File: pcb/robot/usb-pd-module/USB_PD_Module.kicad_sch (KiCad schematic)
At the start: 57 parts, among them J4 USB4151-GF-C, J9 Conn_01x16, U11 MAX77958EWV+T, U15 TPD1E05U06, U16 fpf1048bucx, U17 TPS61253AYFFT, U19 TPD1E05U06, U20 TPD1E05U06, U21 TPD1E05U06, U22 TPD1E05U06, U23 TPD1E05U06, U24 TVS0500DRV

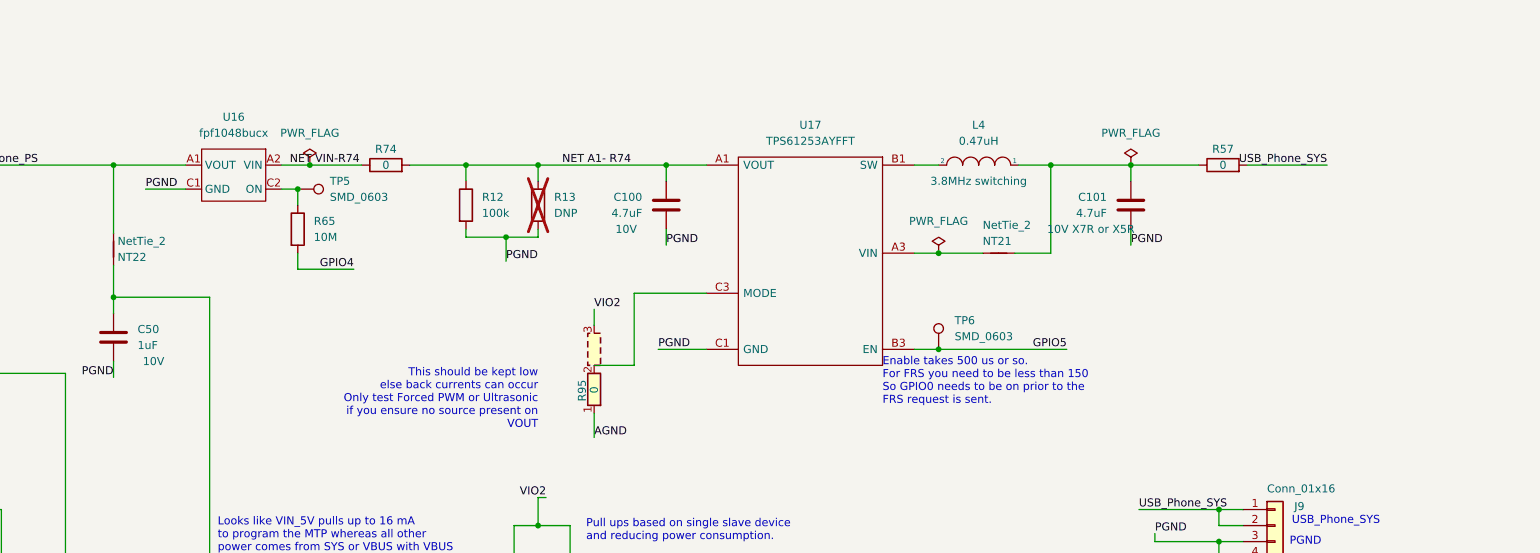
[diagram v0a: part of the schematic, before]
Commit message: Added the TPS22950CDDCR
Generation, upgrade, and replacement of devices in BOM for manufacturing at JLCPCB.
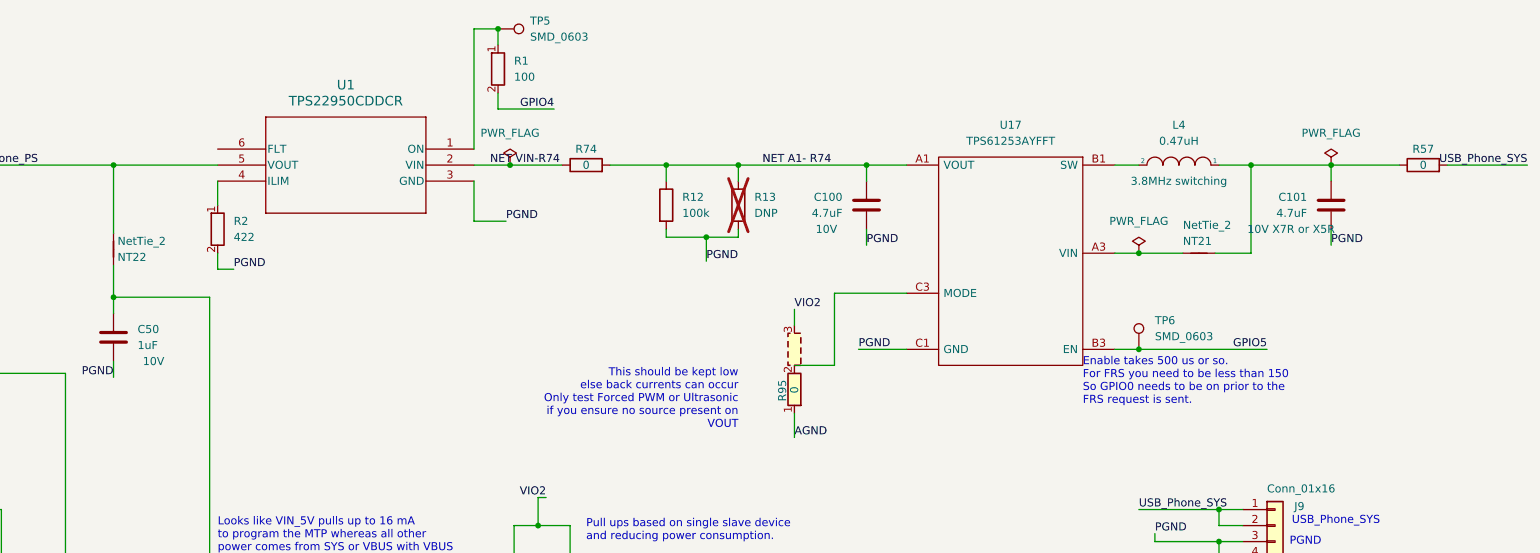
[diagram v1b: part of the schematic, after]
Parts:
- removed R65: 10M, robot:R_0603_1608Metric, symbol robot:R
- removed U16: fpf1048bucx, robot:BGA6N50P3X2_146X96X62N, symbol robot:fpf1048bucx
- added R1: 100, robot:R_0402_1005Metric, symbol robot:RC0402FR-07100RL
- added R2: 422, robot:R_0402_1005Metric, symbol robot:RC0402FR-07422RL
- added U1: TPS22950CDDCR, DDC6_TEX, symbol TPS22950CDDCR:TPS22950CDDCR
- J9: now left out of the parts list
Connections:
- net GND: now also R2.2, U1.3 (GND)
- net GPIO4: now also R1.2
- net NET VIN-R74: now also U1.2 (VIN)
- net VBUS_Phone_PS: now also U1.5 (VOUT)
- net at TP5.1: now also R1.1, U1.1 (ON)
- new net: R2.1, U1.4 (ILIM)
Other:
- moved on the sheet: C100, C101, L4, NT21, R12, R13, R57, R74, R95, TP5, TP6, U17
